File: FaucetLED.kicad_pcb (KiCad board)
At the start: 2 copper layers, 29.2 x 33.3 mm, 25 parts, among them P1 CONN_01X13, P2 CONN_01X02, U1 MAX4256

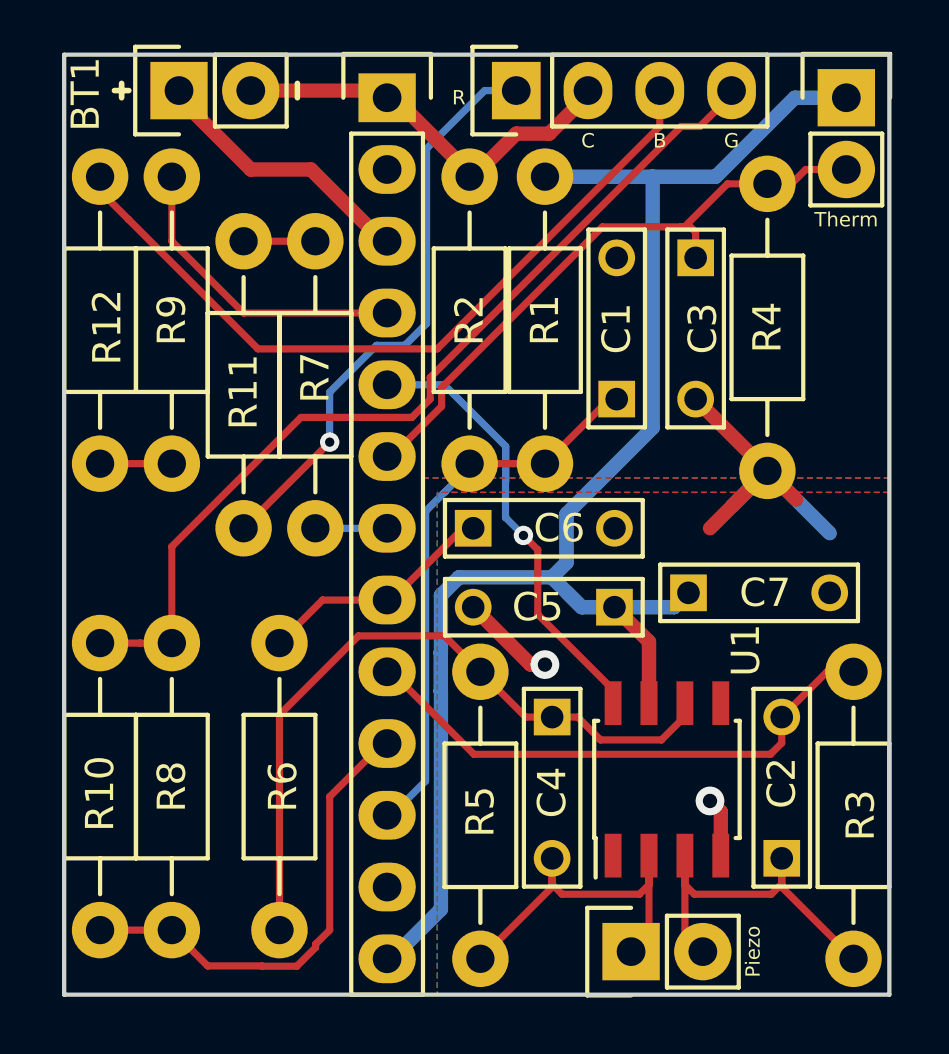
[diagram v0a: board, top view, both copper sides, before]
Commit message: Rotate amplifier circuit so piezo is on right side
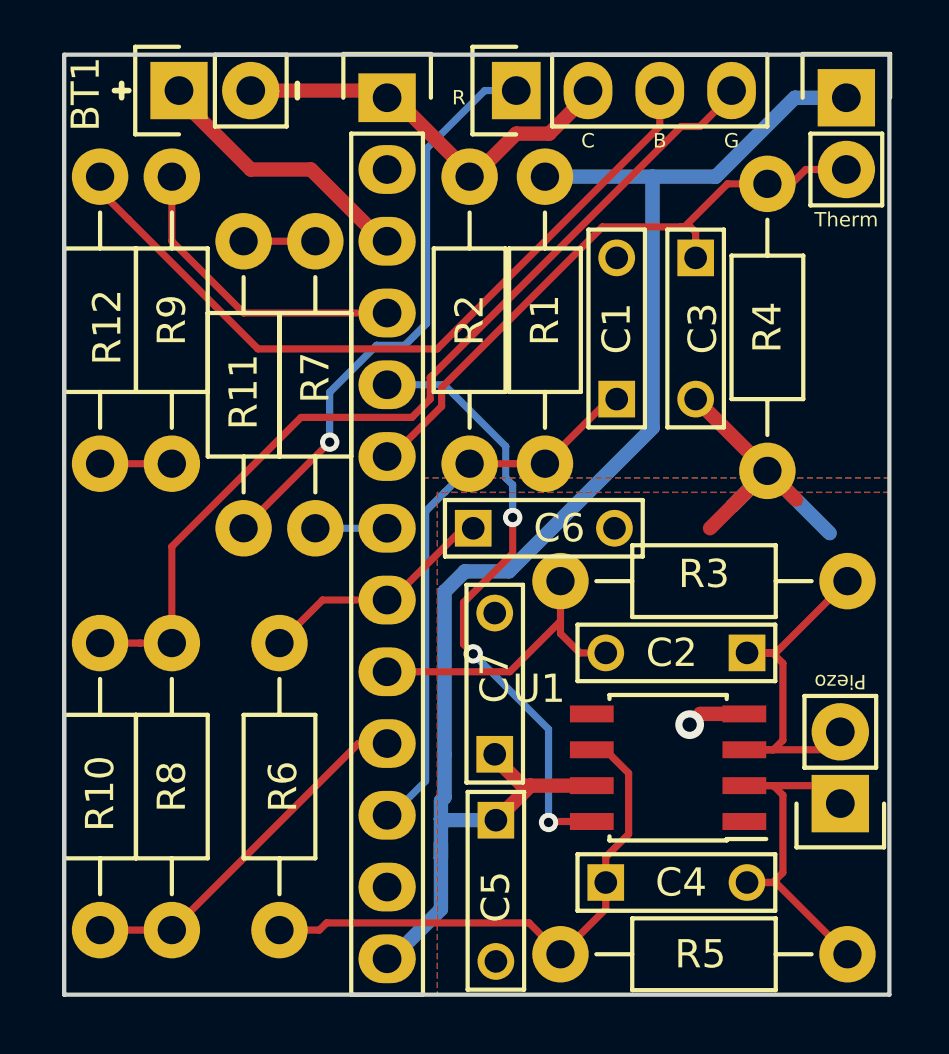
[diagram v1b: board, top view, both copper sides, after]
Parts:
- moved R3 13.4 mm to (129.3, 94.8), turned to 180 degrees
- moved R5 10.4 mm to (119.2, 108.0), turned to 0 degrees
- moved P2 9.07 mm to (129.1, 102.7), turned to 180 degrees
- moved C7 8.93 mm to (116.8, 101.0), turned to 90 degrees
- moved C5 8.63 mm to (116.9, 103.3), turned to 270 degrees
- moved C2 7.38 mm to (125.8, 97.4), turned to 180 degrees
- moved C4 6.16 mm to (120.8, 105.5), turned to 0 degrees
- moved U1 0.42 mm to (123.0, 101.4), turned to 180 degrees
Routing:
- net /VCC_2_BUF: track 19.5 -> 11.7 mm
- net /AMP_SHDN: track 15.9 -> 22.7 mm, vias 1 -> 3
- net Net-(C4-Pad1): track 25.5 -> 20.2 mm
- net /LED_G: track 17.3 -> 13.6 mm
- net GND: track 32.8 -> 29.5 mm, vias 2 -> 1
- net +3V3: track 55.7 -> 52.8 mm

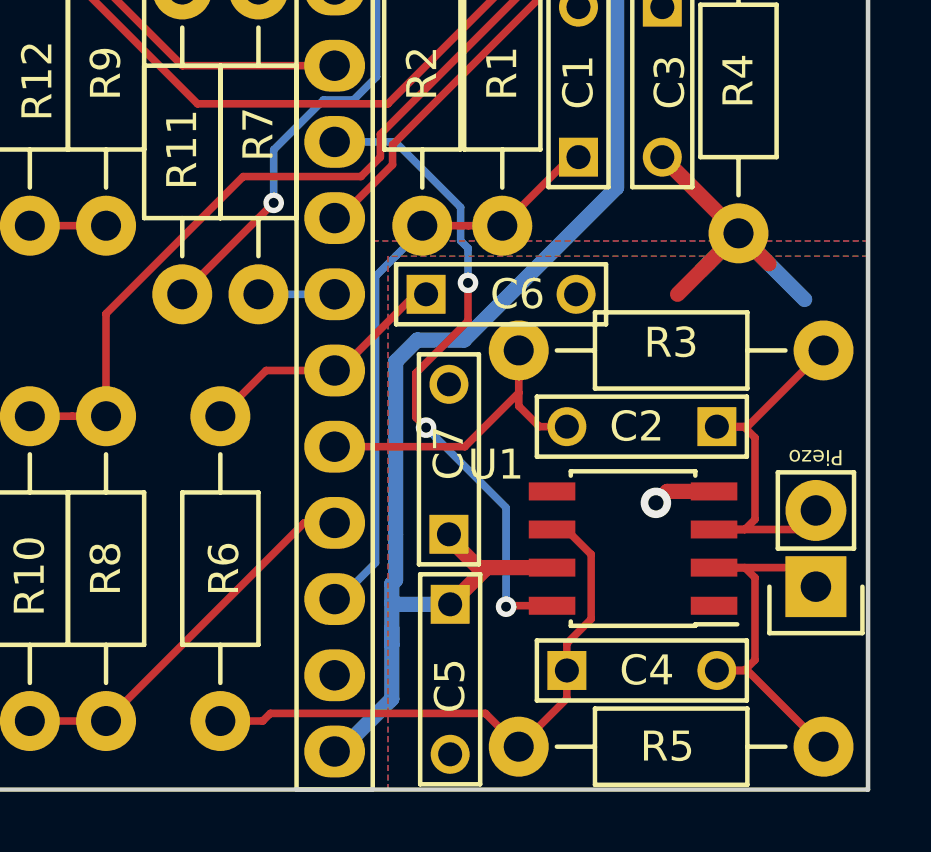
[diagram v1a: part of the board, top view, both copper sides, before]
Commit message: Rotated amplifier another 90 degrees so piezo input is in the middle
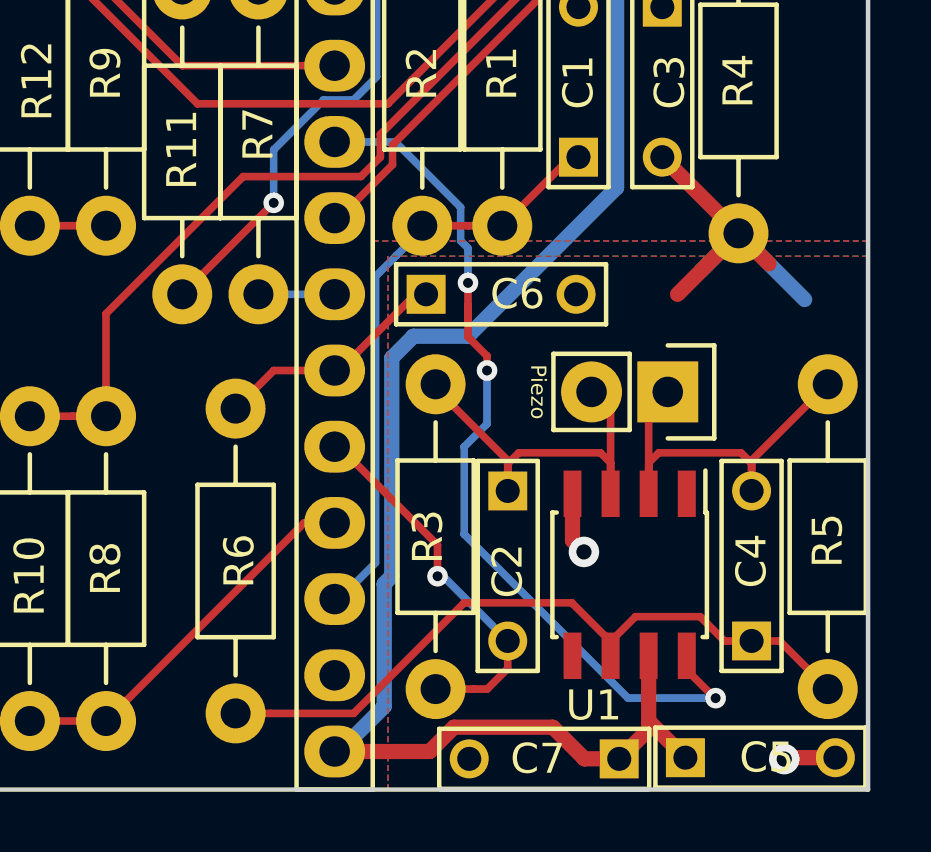
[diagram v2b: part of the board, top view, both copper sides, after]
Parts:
- moved R3 13.0 mm to (116.4, 96.0), turned to 270 degrees
- moved R5 10.5 mm to (129.5, 106.1), turned to 90 degrees
- moved C7 9.39 mm to (122.5, 108.5), turned to 180 degrees
- moved C5 9.36 mm to (124.7, 108.4), turned to 0 degrees
- moved P2 8.16 mm to (124.1, 96.2), turned to 270 degrees
- moved C2 7.29 mm to (118.8, 99.5), turned to 270 degrees
- moved C4 6.23 mm to (126.9, 104.5), turned to 90 degrees
- moved U1 0.88 mm to (122.9, 102.3), turned to 270 degrees
- moved R6 0.57 mm to (109.7, 96.8)
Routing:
- net +3V3: track 52.8 -> 60.8 mm
- net /AMP_SHDN: track 22.7 -> 29.8 mm
- net Net-(C4-Pad1): track 20.2 -> 24.1 mm
- net /VCC_2_BUF: track 11.7 -> 14.4 mm, vias 0 -> 1
- net GND: track 29.5 -> 31.2 mm, vias 1 -> 2
- net /PIEZO_AMP: track 8.54 -> 7.93 mm

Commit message: Swapped LED and thermistor pins on board
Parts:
- moved D1 11.9 mm to (129.5, 77.9), turned to 0 degrees
- moved TH1 7.75 mm to (121.5, 77.5), turned to 90 degrees
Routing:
- net Net-(D1-Pad1): track 20.7 -> 31.0 mm
- net +3V3: track 60.8 -> 53.1 mm
- net Net-(D1-Pad3): track 27.0 -> 30.9 mm
- net GND: track 31.2 -> 35.1 mm
- net /THERM_2: track 22.4 -> 25.5 mm, vias 0 -> 1
- net Net-(D1-Pad4): track 33.0 -> 33.6 mm

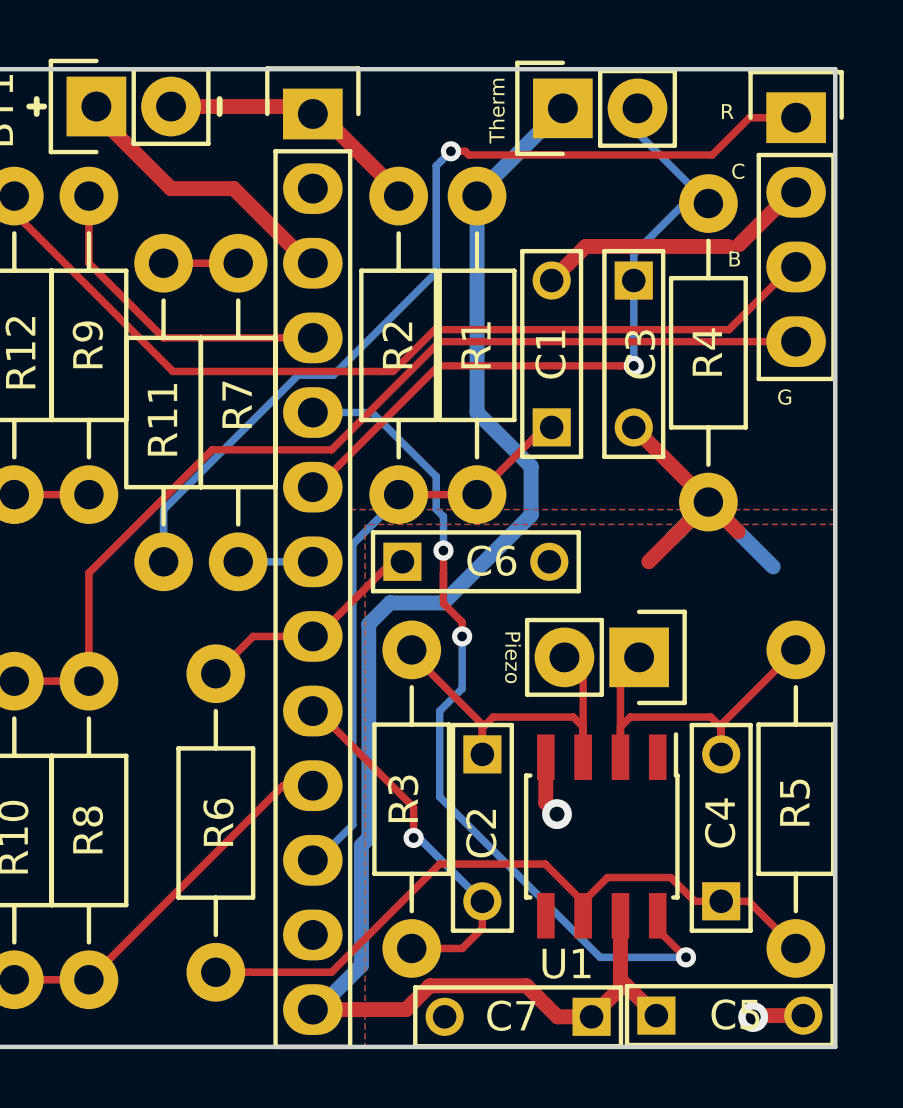
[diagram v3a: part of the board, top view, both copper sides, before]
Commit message: Minor tweaks to spacing around amp circuit
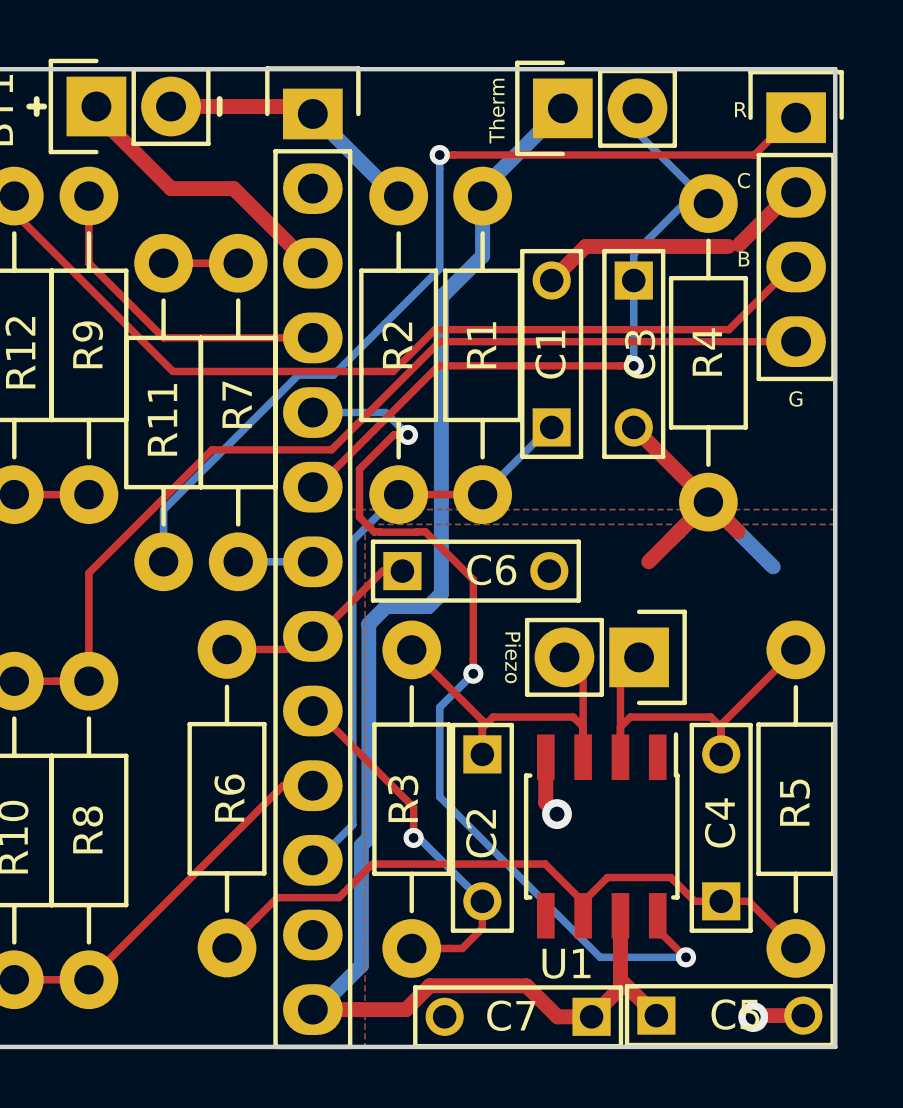
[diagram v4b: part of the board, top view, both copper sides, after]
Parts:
- moved R6 0.91 mm to (110.1, 95.9)
- moved C6 0.32 mm to (116.1, 93.3)
- moved R1 0.19 mm to (118.8, 80.5)
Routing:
- net /AMP_SHDN: track 29.8 -> 32.6 mm
- net +3V3: track 53.1 -> 51.4 mm
- net /PIEZO_AMP: track 7.93 -> 7.07 mm
- net Net-(C4-Pad1): track 24.1 -> 23.4 mm
